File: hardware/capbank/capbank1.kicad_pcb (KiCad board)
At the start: 2 copper layers, 99 x 99 mm, 126 parts, among them J1 Conn_01x03_Socket, J2 Jack-DC, J3 Conn_01x02, J4 Conn_01x02, J6 Conn_01x05, J7 Conn_01x06, K1 3570.1333.121 COMUS, K2 3570.1333.121 COMUS, K4 3570.1333.121 COMUS, SW2 SW_SPST, SW3 SW_DIP_x01, SW4 SW_DIP_x04, U1 ULN2003, U10 TS861IL, U11 NXJ1S1212MC, U12 LM317AEMP, U13 74HC14, U14 MCP1415, U15 MCP1415, U16 LM78L05ACZ, U2 OPA2202IDR, U3 MCP1525-TO, U4 MCP4921-EP, U5 PAI130M61, U6 ATtiny84A-P, U7 4046, U8 M24C16-RMN6TP, U9 LM78L05ACZ

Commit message: KiCad changes
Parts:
- removed C36: 100n, PCM_Capacitor_SMD_AKL:C_0603_1608Metric
- removed J1: Conn_01x03_Socket, Connector_PinHeader_2.54mm:PinHeader_1x03_P2.54mm_Vertical
- removed J6: Conn_01x05, Connector_PinHeader_2.54mm:PinHeader_1x05_P2.54mm_Vertical
- removed SW3: SW_DIP_x01, Button_Switch_THT:SW_DIP_SPSTx01_Slide_9.78x4.72mm_W7.62mm_P2.54mm
- removed U8: M24C16-RMN6TP, Package_SO:SOIC-8_3.9x4.9mm_P1.27mm
- added D10: LED, PCM_Diode_SMD_Handsoldering_AKL:D_0603_1608Metric, F.Cu at (63.6, 122.6)
- added D11: LED, PCM_Diode_SMD_Handsoldering_AKL:D_0603_1608Metric, F.Cu at (63.6, 125.7)
- added D8: LED, PCM_Diode_SMD_Handsoldering_AKL:D_0603_1608Metric, F.Cu at (52.5, 126.8)
- added D9: LED, PCM_Diode_SMD_Handsoldering_AKL:D_0603_1608Metric, F.Cu at (63.6, 119.5)
- added J5: Conn_01x06, Connector_PinHeader_2.54mm:PinHeader_1x06_P2.54mm_Vertical, F.Cu at (48.1, 120.2)
- added JP5: 0, PCM_Resistor_SMD_AKL:R_0603_1608Metric, F.Cu at (113.4, 60.0)
- added JP6: 0, PCM_Resistor_SMD_AKL:R_0603_1608Metric, F.Cu at (113.4, 62.8)
- added R11: 1k, PCM_Resistor_SMD_AKL:R_0603_1608Metric, F.Cu at (67.7, 119.3)
- added R12: 1k, PCM_Resistor_SMD_AKL:R_0603_1608Metric, F.Cu at (67.7, 122.0)
- added R4: 1k, PCM_Resistor_SMD_AKL:R_0603_1608Metric, F.Cu at (52.5, 123.9)
- added TP23: ~, TestPoint:TestPoint_THTPad_1.5x1.5mm_Drill0.7mm, F.Cu at (52.2, 130.1)
- added Y1: 16MHz, Crystal:Resonator-3Pin_W7.0mm_H2.5mm, F.Cu at (52.5, 120.2)
- C40, C41: value C -> 1n
- R13: value 10k -> 22k
- R16: value 10k -> 1k
- R2: value 50k -> 110k
- moved R16 53.1 mm to (67.7, 124.8)
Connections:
- net /Relays/RELAY_CTRL_1 renamed /Relays/RELAY1_LED
- net /Relays/RELAY_CTRL_2 renamed /Relays/RELAY2_LED
- C41 pad 1: Net-(C41-Pad1) -> Net-(U7-VCOin)
- R15 pad 1: Net-(U7-PC1) -> Net-(JP5-B)
- R16 pad 1: Net-(U7-VCOin) -> /Relays/RELAY3_LED
- R16 pad 2: Net-(C41-Pad1) -> Net-(D11-A)
- R8 pad 2: Net-(J1-Pin_1) -> /Microcontroller/~{RESET}
- SW2 pad 2: Net-(J1-Pin_1) -> /Microcontroller/~{RESET}
- TP7 pad 1: /Relays/RELAY_CTRL_3 -> /Relays/RELAY3_LED
- U1 pad 7: /Relays/RELAY_CTRL_3 -> /Relays/RELAY3_LED
- U6 pad 7: /Microcontroller/PRG_MOSI_I2C_SDA -> /Microcontroller/PRG_MOSI_LED
- U6 pad 9: /Microcontroller/PRG_SCK_I2C_SCL -> /Microcontroller/PRG_SCK_FREE
- U7 pad 13: unconnected-(U7-PC2-Pad13) -> Net-(JP5-A)
- U7 pad 2: Net-(U7-PC1) -> Net-(JP6-A)

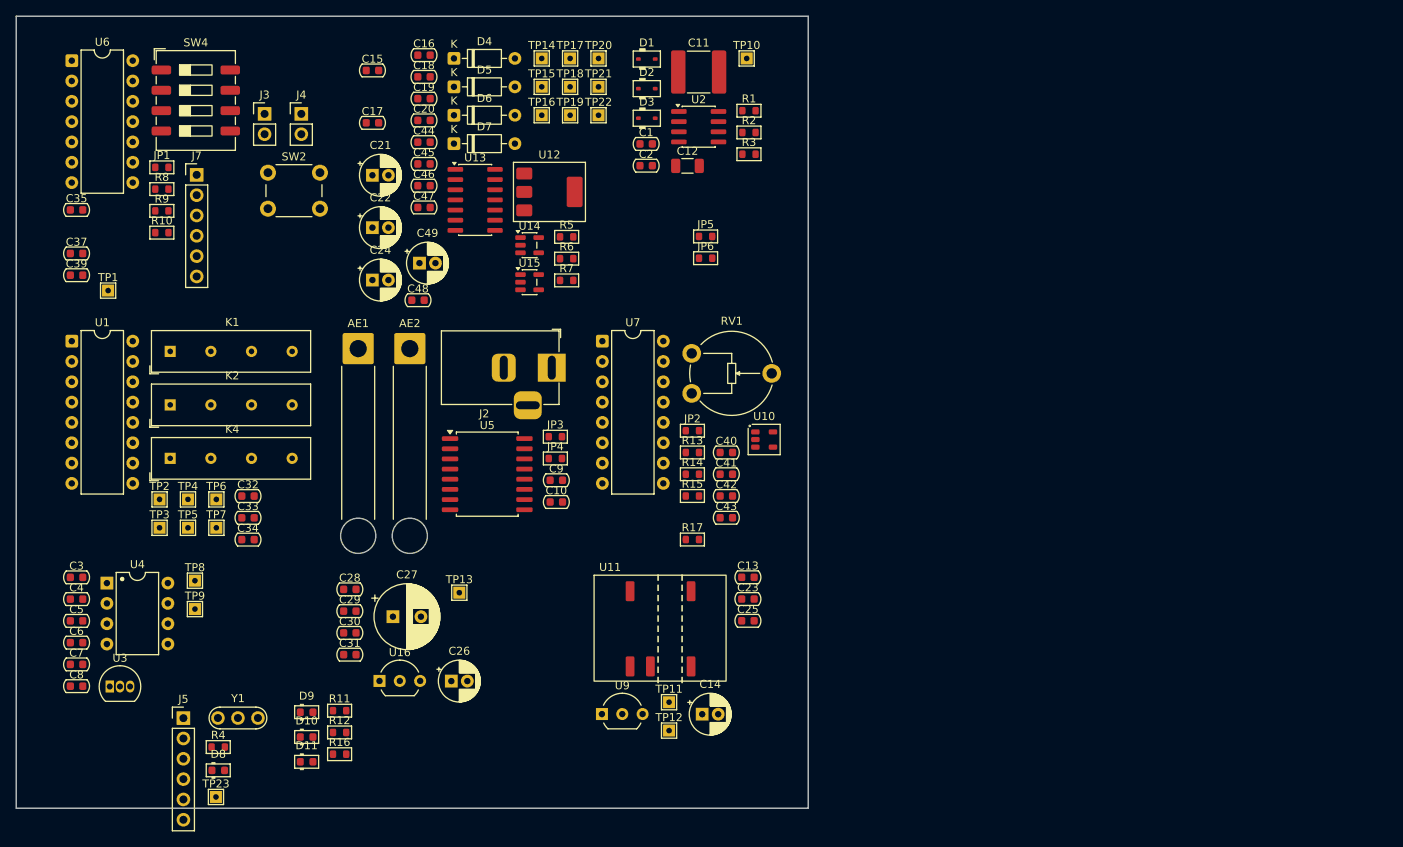
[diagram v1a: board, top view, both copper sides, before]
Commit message: Progress, layout nearly completed, build oscillator on breadboard
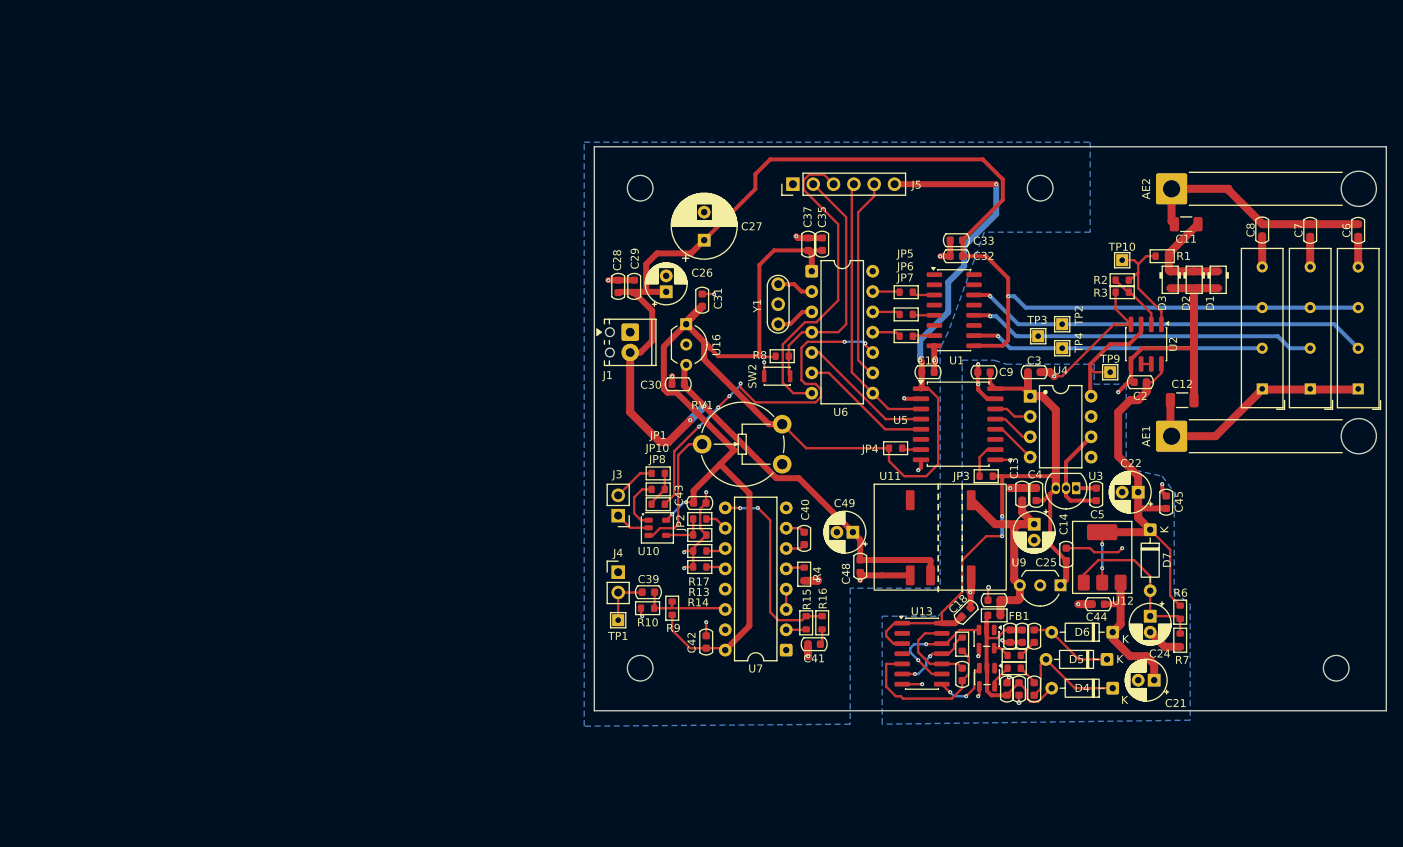
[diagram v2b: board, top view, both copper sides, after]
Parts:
- removed C1: 1p, PCM_Capacitor_SMD_AKL:C_0603_1608Metric
- removed C34: 100n, PCM_Capacitor_SMD_AKL:C_0603_1608Metric
- removed D10, D11, D8, D9: LED, PCM_Diode_SMD_Handsoldering_AKL:D_0603_1608Metric
- removed J2: Jack-DC, Connector_BarrelJack:BarrelJack_Horizontal
- removed J7: Conn_01x06, Connector_PinHeader_2.54mm:PinHeader_1x06_P2.54mm_Vertical
- removed SW4: SW_DIP_x04, Button_Switch_SMD:SW_DIP_SPSTx04_Slide_9.78x12.34mm_W8.61mm_P2.54mm
- removed TP11, TP12, TP13, TP14, TP15, TP16, TP17, TP18, TP19, TP20, TP21, TP22, TP23, TP5, TP6, TP7, TP8: ~, TestPoint:TestPoint_THTPad_1.5x1.5mm_Drill0.7mm
- added FB1: Ferrite_Bead, PCM_Ferrite_SMD_AKL:Ferrite_0603_1608Metric, F.Cu at (149.5, 107.4)
- added H1: MountingHole, MountingHole:MountingHole_3.2mm_M3, F.Cu at (192.2, 114.0)
- added H2: MountingHole, MountingHole:MountingHole_3.2mm_M3, F.Cu at (155.2, 54.0)
- added H3: MountingHole, MountingHole:MountingHole_3.2mm_M3, F.Cu at (105.2, 114.0)
- added H4: MountingHole, MountingHole:MountingHole_3.2mm_M3, F.Cu at (105.2, 54.0)
- added J1: Screws, TerminalBlock_Phoenix:TerminalBlock_Phoenix_MPT-0,5-2-2.54_1x02_P2.54mm_Horizontal, F.Cu at (104.0, 72.0)
- added JP10: 0, PCM_Resistor_SMD_AKL:R_0603_1608Metric, F.Cu at (107.5, 91.7)
- added JP7: 0, PCM_Resistor_SMD_AKL:R_0603_1608Metric, F.Cu at (138.5, 72.5)
- added JP8: 0, PCM_Resistor_SMD_AKL:R_0603_1608Metric, F.Cu at (107.5, 93.5)
- C11: footprint Capacitor_SMD:C_2220_5750Metric -> Capacitor_SMD:C_1206_3216Metric
- C33: value 100n -> 1u
- C40: value 1n -> 120p
- C41: value 1n -> C
- R11, R12: value 1k -> 22
- R13: value 22k -> 10k
- R16, R4: value 1k -> 10k
- R2: value 110k -> 50k
- SW2: footprint Button_Switch_THT:SW_PUSH_6mm -> Button_Switch_SMD:SW_SPST_CK_KXT3
- U1: footprint Package_DIP:DIP-16_W7.62mm -> Package_SO:SOIC-16_3.9x9.9mm_P1.27mm
- moved C6 168.3 mm to (195.0, 59.3), turned to 90 degrees
- moved C7 163.5 mm to (189.0, 59.3), turned to 90 degrees
- moved C8 158.8 mm to (183.0, 59.2), turned to 90 degrees
- moved K4 148.7 mm to (195.0, 79.1), turned to 90 degrees
- moved K1 142.6 mm to (189.0, 79.1), turned to 90 degrees
- moved K2 136.5 mm to (183.0, 79.1), turned to 90 degrees
- moved C5 128.4 mm to (162.2, 92.3), turned to 90 degrees
- moved U3 123.3 mm to (159.8, 91.5), turned to 180 degrees
- moved C3 122.4 mm to (154.5, 77.0)
- moved C4 120.7 mm to (154.8, 92.3), turned to 90 degrees
- moved TP9 118.2 mm to (164.0, 77.0)
- moved U4 117.8 mm to (154.0, 80.0)
- moved C21 116.3 mm to (169.5, 115.5), turned to 180 degrees
- moved TP2 114.9 mm to (158.0, 71.0)
- moved D4 113.9 mm to (164.3, 116.5), turned to 180 degrees
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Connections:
- net /Microcontroller/PRG_SCK_FREE renamed /Microcontroller/PRG_SCK_I2C_SCL
- C15 pad 2: /BiasSupply/DRIVE -> Net-(C15-Pad2)
- C17 pad 2: /BiasSupply/~{DRIVE} -> Net-(C17-Pad2)
- C19 pad 1: V_SUPPLY_ISOL -> Net-(D4-A)
- C2 pad 1: V_ISOL_CLEAN -> HV_CLEAN
- C20 pad 1: V_SUPPLY_ISOL -> Net-(D4-A)
- C41 pad 1: Net-(U7-VCOin) -> Net-(C41-Pad1)
- C46 pad 1: V_SUPPLY_ISOL -> Net-(D4-A)
- C47 pad 1: V_SUPPLY_ISOL -> Net-(D4-A)
- D4 pad 2: V_SUPPLY_ISOL -> Net-(D4-A)
- J5 pad 3: /Microcontroller/PRG_MOSI_LED -> /Microcontroller/PRG_MOSI_I2C_SDA
- J5 pad 4: /Microcontroller/PRG_MISO_SPI_CS -> /~{CS}
- JP5 pad 1: Net-(JP5-A) -> /Microcontroller/HVSP_SDI_RELAY1
- JP5 pad 2: Net-(JP5-B) -> /Microcontroller/RELAY1
- JP6 pad 1: Net-(JP6-A) -> /Microcontroller/HVSP_SII_RELAY2
- JP6 pad 2: Net-(JP5-B) -> /Microcontroller/RELAY2
- K1 pad 3: Net-(U1-O4) -> Net-(U1-O5)
- K4 pad 3: Net-(U1-O1) -> Net-(U1-O3)
- R11 pad 1: /Relays/RELAY1_LED -> Net-(C15-Pad2)
- R11 pad 2: Net-(D9-A) -> /BiasSupply/DRIVE
- R12 pad 1: /Relays/RELAY2_LED -> Net-(C17-Pad2)
- R12 pad 2: Net-(D10-A) -> /BiasSupply/~{DRIVE}
- R15 pad 1: Net-(JP5-B) -> Net-(U7-PC1)
- R16 pad 1: /Relays/RELAY3_LED -> Net-(U7-VCOin)
- R16 pad 2: Net-(D11-A) -> Net-(C41-Pad1)
- R4 pad 1: /Microcontroller/PRG_MOSI_LED -> Net-(U7-Inh)
- R4 pad 2: Net-(D8-A) -> GND
- TP2 pad 1: Net-(U1-O1) -> Net-(U1-O3)
- TP3 pad 1: Net-(U1-O4) -> Net-(U1-O5)
- U1 pad 1: /Relays/RELAY1_LED -> unconnected-(U1-I1-Pad1)
- U1 pad 12: unconnected-(U1-O5-Pad12) -> Net-(U1-O5)
- U1 pad 13: Net-(U1-O4) -> unconnected-(U1-O4-Pad13)
- U1 pad 14: unconnected-(U1-O3-Pad14) -> Net-(U1-O3)
- U1 pad 16: Net-(U1-O1) -> unconnected-(U1-O1-Pad16)
- U1 pad 3: unconnected-(U1-I3-Pad3) -> /Microcontroller/RELAY1
- U1 pad 4: /Relays/RELAY2_LED -> unconnected-(U1-I4-Pad4)
- U1 pad 5: unconnected-(U1-I5-Pad5) -> /Microcontroller/RELAY2
- U1 pad 7: /Relays/RELAY3_LED -> /Microcontroller/RELAY3
- U10 pad 1: /Microcontroller/FSK_CMP -> /Microcontroller/FSK Demod/FSK_CMP
- U13 pad 1: Net-(R5-Pad2) -> VDD_ISOL
- U13 pad 10: unconnected-(U13-Pad10) -> Net-(C16-Pad2)
- U13 pad 11: VDD_ISOL -> Net-(R5-Pad2)
- U13 pad 2: Net-(C16-Pad2) -> unconnected-(U13-Pad2)
- U13 pad 3: Net-(C16-Pad1) -> VDD_ISOL
- U13 pad 4: Net-(R5-Pad2) -> unconnected-(U13-Pad4)
- U13 pad 5: VDD_ISOL -> Net-(C16-Pad1)
- U13 pad 6: unconnected-(U13-Pad6) -> Net-(R5-Pad2)
- U14 pad 2: V_SUPPLY_ISOL -> Net-(D4-A)
- U15 pad 2: V_SUPPLY_ISOL -> Net-(D4-A)
- U2 pad 3: /Isolated/Varactor/VTUNE -> /Isolated/VTUNE
- U2 pad 5: GNDREF -> GND_ISOL
- U2 pad 8: V_ISOL_CLEAN -> HV_CLEAN
- U5 pad 12: /ISOL_~{CS} -> /ISOL_SDI
- U5 pad 13: /ISOL_SDI -> /ISOL_SCK
- U5 pad 14: /ISOL_SCK -> /ISOL_~{CS}
- U5 pad 3: /SCK -> /~{CS}
- U5 pad 4: /SDI -> /SCK
- U5 pad 5: /~{CS} -> /SDI
- U6 pad 5: /Microcontroller/SPI_SCK -> /SCK
- U6 pad 6: /Microcontroller/SPI_MOSI -> /SDI
- U6 pad 7: /Microcontroller/PRG_MOSI_LED -> /Microcontroller/PRG_MOSI_I2C_SDA
- U6 pad 8: /Microcontroller/PRG_MISO_SPI_CS -> /~{CS}
- U7 pad 13: Net-(JP5-A) -> unconnected-(U7-PC2-Pad13)
- U7 pad 2: Net-(JP6-A) -> Net-(U7-PC1)
- U7 pad 5: unconnected-(U7-Inh-Pad5) -> Net-(U7-Inh)
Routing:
- net V_SUPPLY: track 0.00 -> 213.2 mm, vias 0 -> 3
- net VDD: track 0.00 -> 201.5 mm, vias 0 -> 4
- net GND_ISOL: track 0.00 -> 100.1 mm, vias 0 -> 17
- net VDD_ISOL: track 0.00 -> 84.5 mm, vias 0 -> 2
- net HV_CLEAN: track 0.00 -> 52.6 mm, vias 0 -> 2
- net GND: track 0.00 -> 51.9 mm, vias 0 -> 17
- net Net-(U1-O3): track 0.00 -> 50.8 mm, vias 0 -> 1
- net /Microcontroller/HVSP_CLK_FSK_IN: track 0.00 -> 48.4 mm, vias 0 -> 6
- net Net-(U1-O5): track 0.00 -> 44.0 mm, vias 0 -> 1
- net /Microcontroller/PRG_MOSI_I2C_SDA: track 0.00 -> 39.5 mm
- net Net-(U1-O7): track 0.00 -> 36.7 mm, vias 0 -> 1
- net /~{CS}: track 0.00 -> 34.2 mm
- net /Microcontroller/~{RESET}: track 0.00 -> 31.4 mm
- net /Isolated/ANT1: track 0.00 -> 30.3 mm
- net /Isolated/ANT2: track 0.00 -> 29.8 mm
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- added copper zone on B.Cu, net GND
- added copper zone on B.Cu, net GND_ISOL
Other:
- board size 99 x 99 mm -> 99 x 70.5 mm
